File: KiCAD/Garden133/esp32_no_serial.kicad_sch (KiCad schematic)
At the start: 13 parts, among them J1 USB_B_Micro, J2 Edge2x6_Connector, U3 ESP32-WROOM-32, U4 NCP114ASN330T1G

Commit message: Board version 5
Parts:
- removed DUSB1: SS14, Diode_SMD:D_2010_5025Metric, symbol Diode:1N5819
- removed F1: 0.5A, Diode_SMD:D_0805_2012Metric, symbol Device:Fuse_Small
- renumbered Ca1 to Ca6, Ca2 to Ca7, Cb2 to Cb1, Cm1 to Cu1, Cm2 to Cu2, Ru1 to Ru7, U4 to U3, U3 to U4
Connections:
- net GPIO26: now reaches U4.26 (IO4)
- net ADC1_CH6: now reaches U4.6 (IO34)
- net ADC1_CH7: now reaches U4.7 (IO35)
- net GPIO33 renamed ADC1_CH5
- no-connect marks 22 -> 19

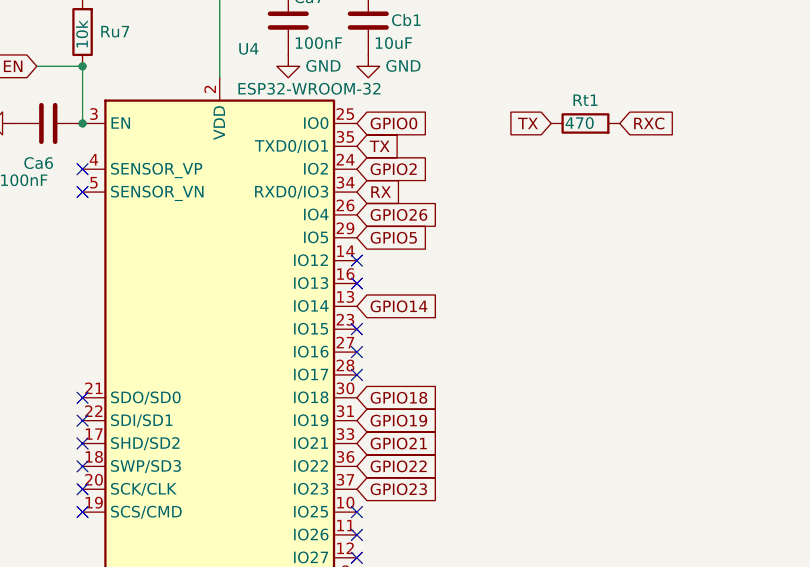
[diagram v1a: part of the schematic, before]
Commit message: Update for board v6
- Added OpenSCAD models for Solar panel mount, tray for board+battery
- ADC Adjustment because using 220k resistors, not 200k.
- Licenses updated
- Remove support for v4 boards, update ADC slopes
- Board v6.0 (ordered)
- Support publishing more data via LoRa.
  Not able to include solar, due to packet size limitations.
- og3 version -> 0.3.10
- add raw_counts to packet
- add a filter for the moisture readings
- support normal mode -- deep sleep
  Normal mode is enabled based on the reading of the debug switch
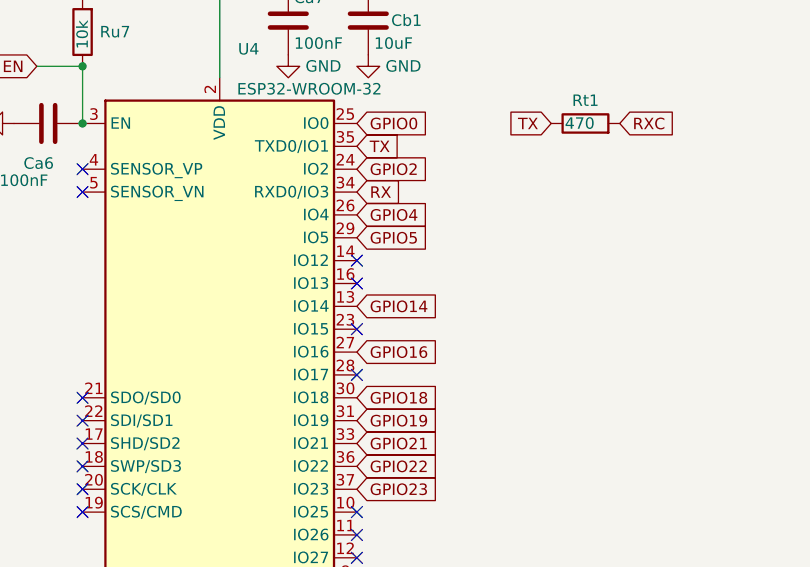
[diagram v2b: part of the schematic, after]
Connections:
- net GPIO16: now reaches U4.27 (IO16)
- net GPIO26 renamed GPIO4
- no-connect marks 19 -> 18
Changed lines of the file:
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@@
-	)
-	(no_connect
-		(at 63.5 71.12)
 	)
 	(no_connect
@@
 		)
 	)
-	(global_label "GPIO26"
+	(global_label "GPIO4"
 		(shape input)
 		(at 63.5 55.88 0)
@@
 		)
 		(property "Intersheetrefs" "${INTERSHEET_REFS}"
-			(at 73.3795 55.88 0)
+			(at 72.17 55.88 0)
 			(effects
 				(font
@@
 			(effects
 				(font
+					(size 1.27 1.27)
+				)
+				(justify left)
+				(hide yes)
+			)
+		)
+	)
+	(global_label "GPIO16"
+		(shape input)
+		(at 63.5 71.12 0)
+		(fields_autoplaced yes)
+		(effects
+			(font
+				(size 1.27 1.27)
+			)
+			(justify left)
+		)
+		(property "Intersheetrefs" "${INTERSHEET_REFS}"
+			(at 73.3795 71.12 0)
+			(effects
+				(font

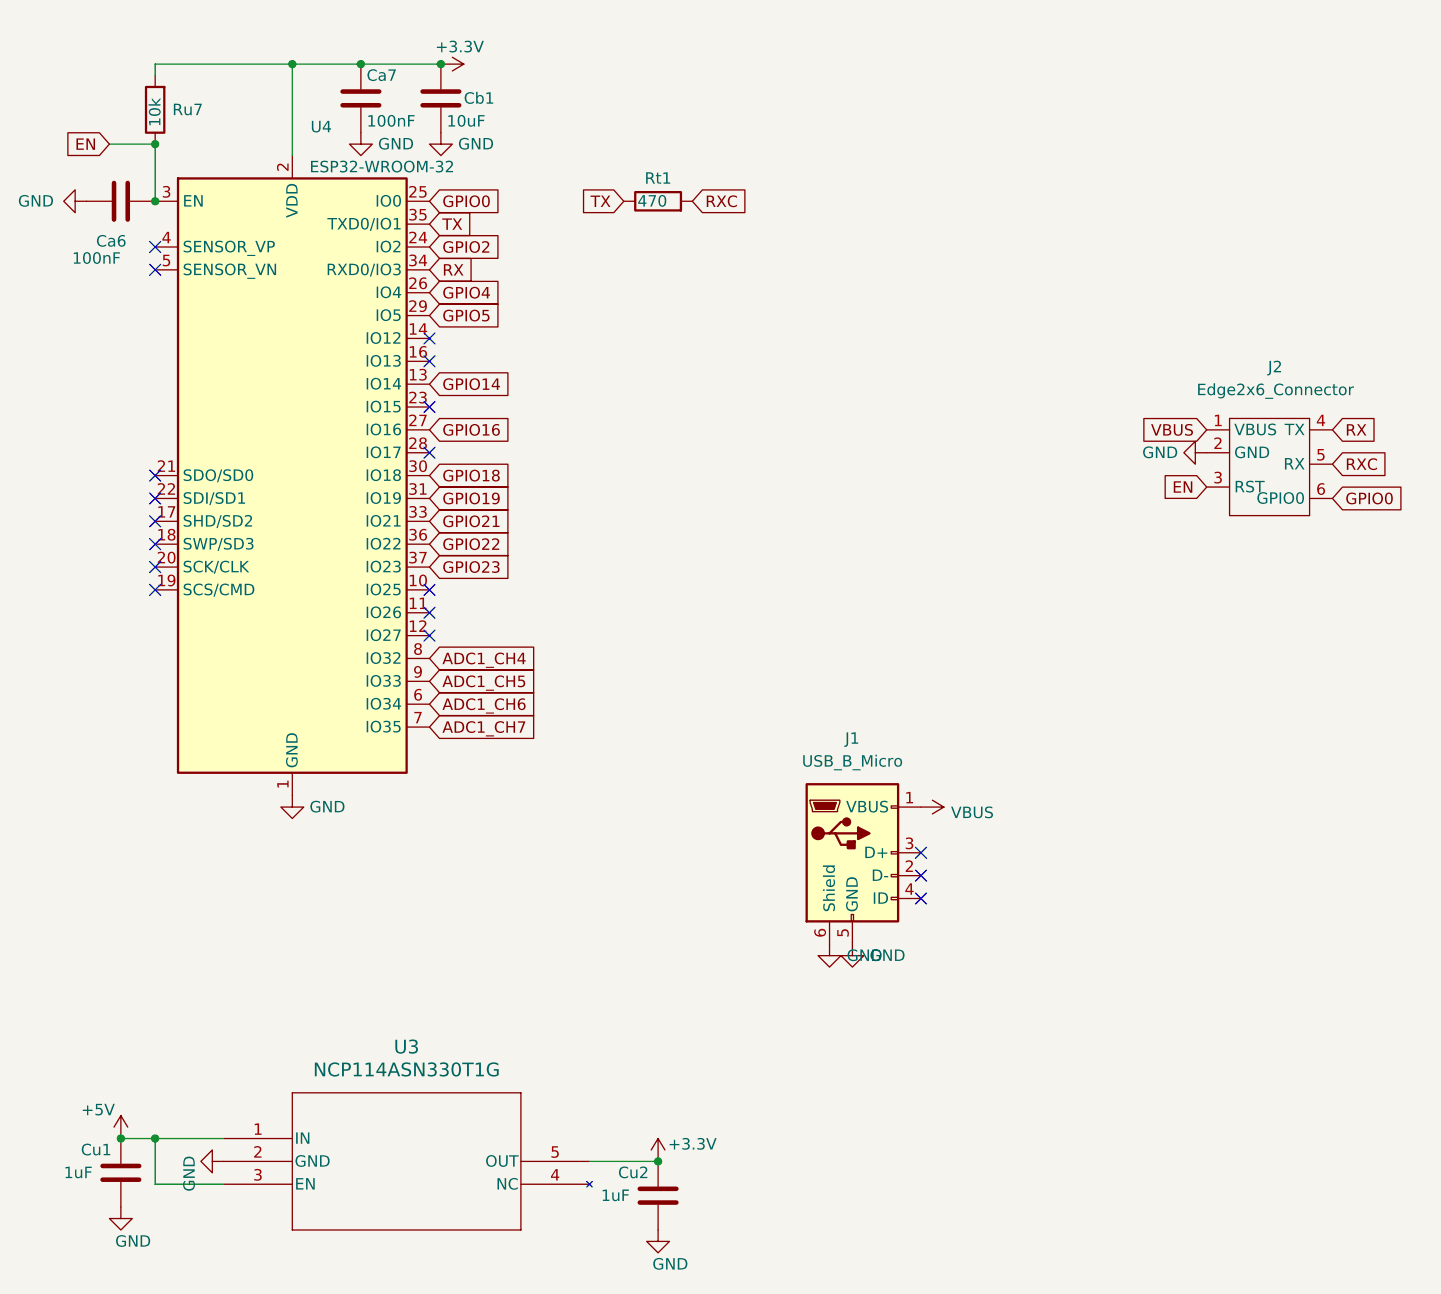
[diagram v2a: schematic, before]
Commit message: Update PCB
- Button controls power to 3.3V LDO
- DIO readings for STDBY and CHRG
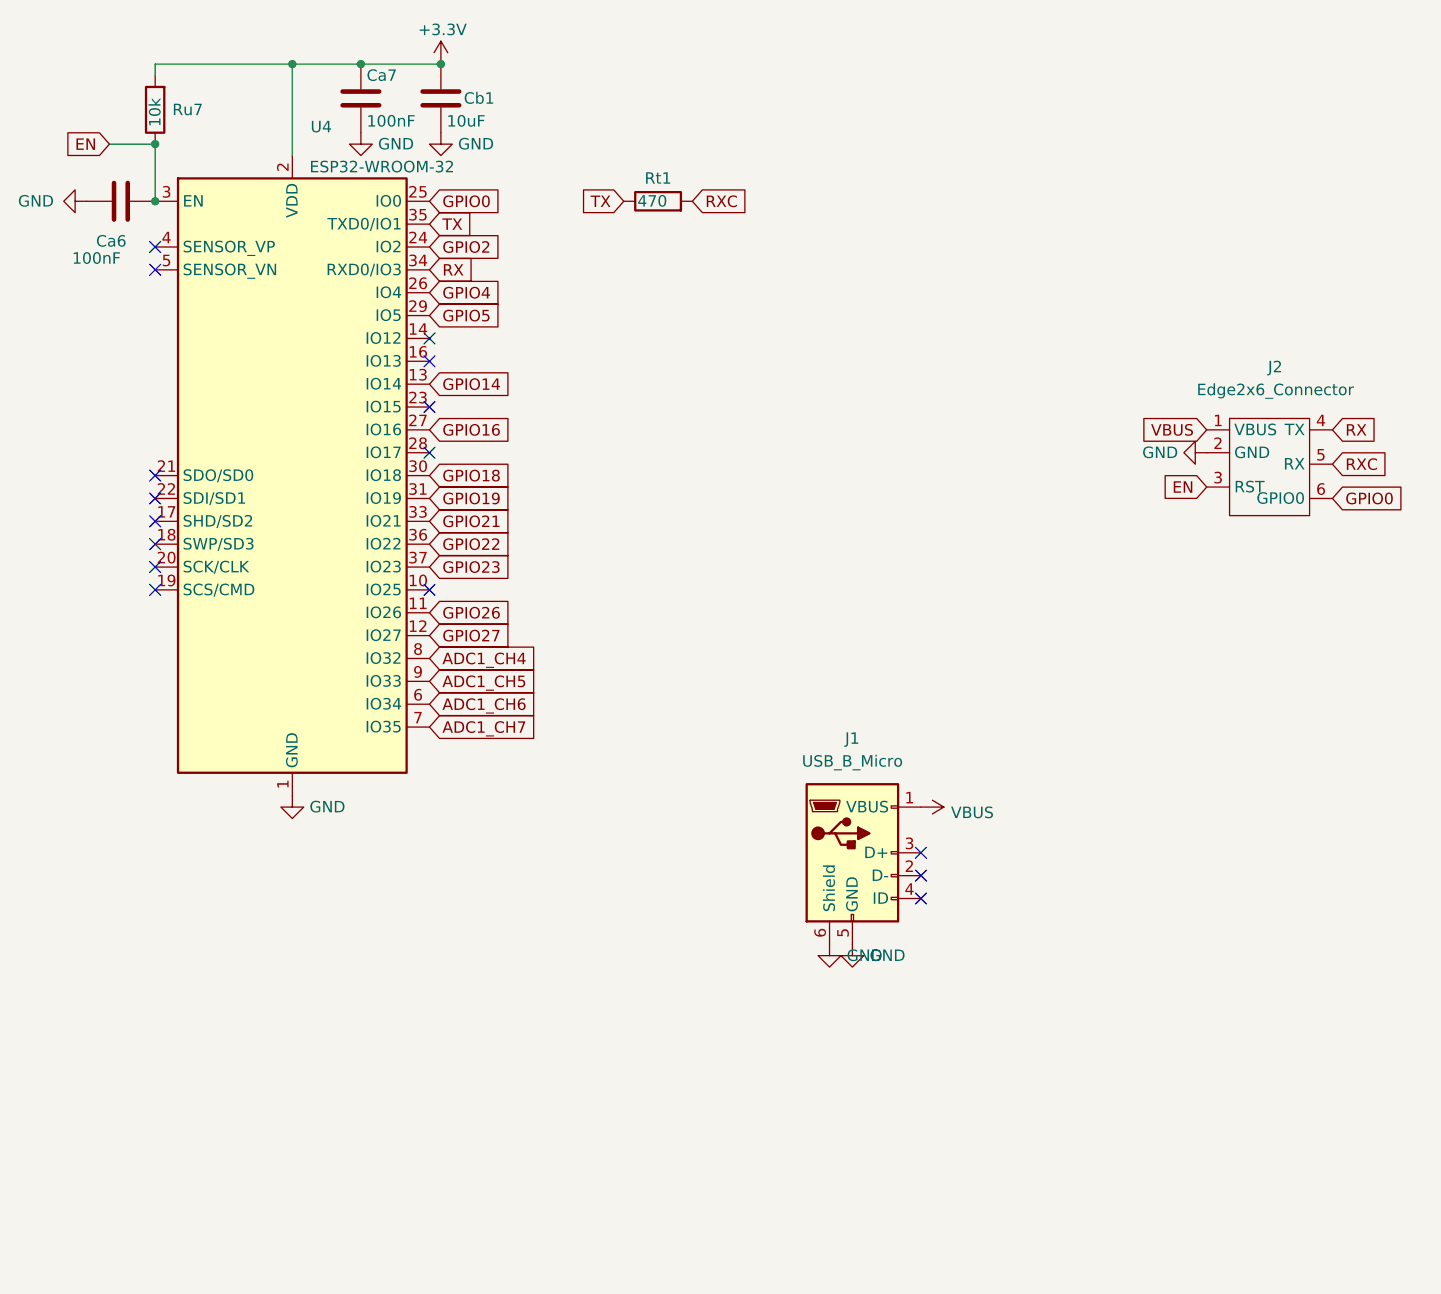
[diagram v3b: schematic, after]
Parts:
- removed Cu1, Cu2: 1uF, Capacitor_SMD:C_0805_2012Metric_Pad1.18x1.45mm_HandSolder, symbol Device:C
- removed U3: NCP114ASN330T1G, Package_TO_SOT_SMD:TSOT-23-5, symbol chl33:NCP114ASN330T1G
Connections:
- net GPIO26: now reaches U4.11 (IO26)
- net GPIO27: now reaches U4.12 (IO27)
- no-connect marks 18 -> 16
